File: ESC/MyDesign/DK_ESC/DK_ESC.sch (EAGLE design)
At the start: 38 parts

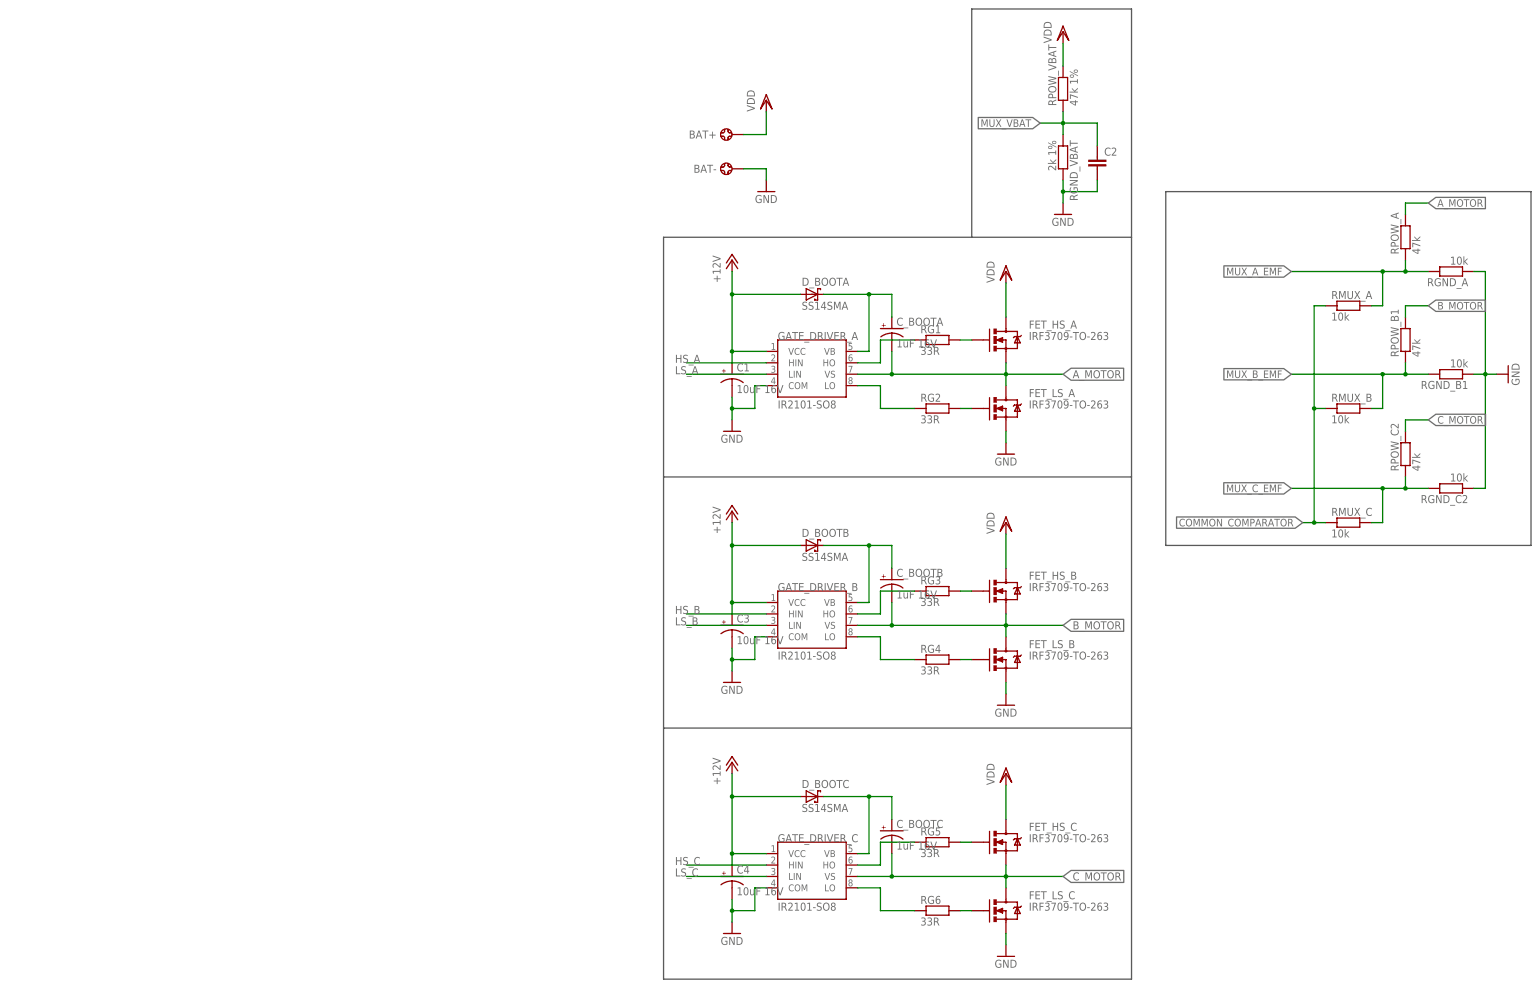
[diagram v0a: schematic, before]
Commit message: ESC Design: include MCU
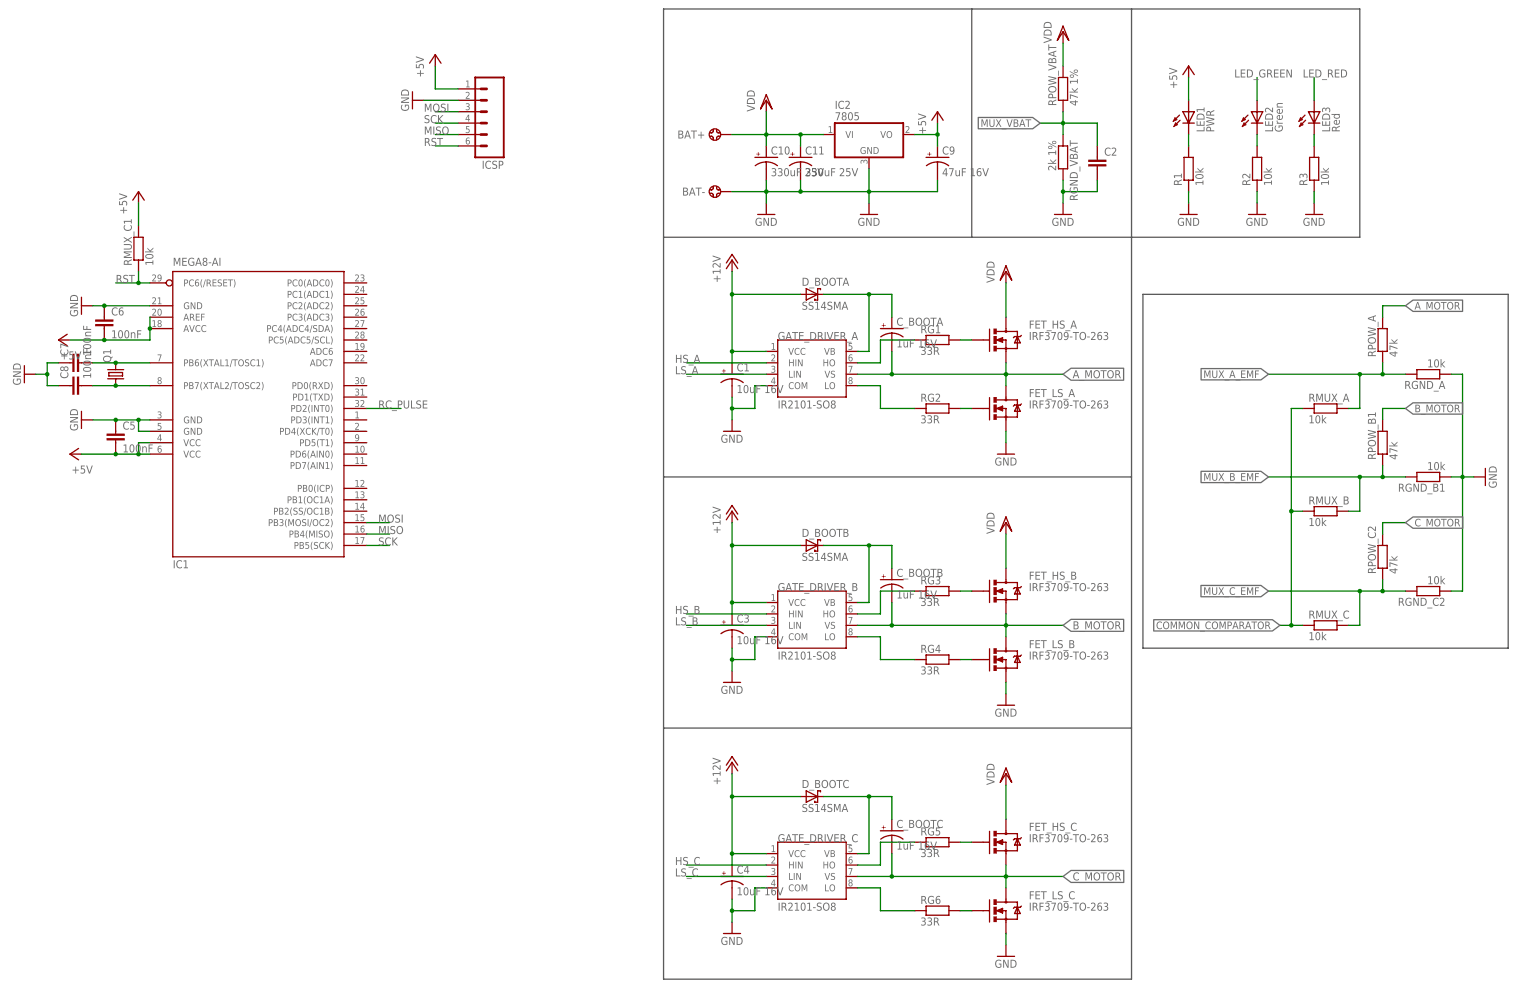
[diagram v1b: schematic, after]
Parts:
- added C10, C11: 330uF 25V, DangKiet:CAP_POLPTH
- added C5, C6, C7, C8: 100nF, RCL:C-SMDC0805K
- added C9: 47uF 16V, RCL:C-TANT-SMDEIA6032
- added IC1: MEGA8-AI, atmel:MEGA8-AI
- added IC2: 7805, Regulator-linear:78XXX-3P05-TO252
- added ICSP: (no value), SparkFun-Connectors:M06NO_SILK_FEMALE_PTH
- added LED1: PWR, LED:LED3MM
- added LED2: Green, LED:LED3MM
- added LED3: Red, LED:LED3MM
- added Q1: (no value), DangKiet:CRYSTALHC49S
- added R1, R2, R3: 10k, RCL:RESISTOR-SMDR0805
- added RMUX_C1: 10k, RCL:RESISTOR-SMDR0603
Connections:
- new net +5V: C5.2, C6.2, C9.+, IC1.AREF, IC1.AVCC, IC1.VCC@1, IC1.VCC@2, IC2.VO, ICSP.1, LED1.A, RMUX_C1.2
- new net LED_GREEN: LED2.A
- new net LED_RED: LED3.A
- new net MISO: IC1.PB4(MISO), ICSP.5
- new net MOSI: IC1.PB3(MOSI/OC2), ICSP.3
- new net N$13: LED1.C, R1.2
- new net N$14: C7.2, IC1.PB6(XTAL1/TOSC1), Q1.2
- new net N$15: C8.2, IC1.PB7(XTAL2/TOSC2), Q1.1
- new net N$16: LED2.C, R2.2
- new net N$17: LED3.C, R3.2
- new net RC_PULSE: IC1.PD2(INT0)
- new net RST: IC1.PC6(/RESET), ICSP.6, RMUX_C1.1
- new net SCK: IC1.PB5(SCK), ICSP.4
- net GND: now also C10.-, C11.-, C5.1, C6.1, C7.1, C8.1, C9.-, IC1.GND, IC1.GND@1, IC1.GND@2, IC2.GND, ICSP.2, R1.1, R2.1, R3.1
- net VDD: now also C10.+, C11.+, IC2.VI
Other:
- note added: "HALF-BRIDGE"
- note added: "POWER SUPPLY"
- moved on the sheet: BAT+, BAT-, RGND_A, RGND_B1, RGND_C2, RMUX_A, RMUX_B, RMUX_C, RPOW_A, RPOW_B1, RPOW_C2

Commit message: Update layout ESC: test version
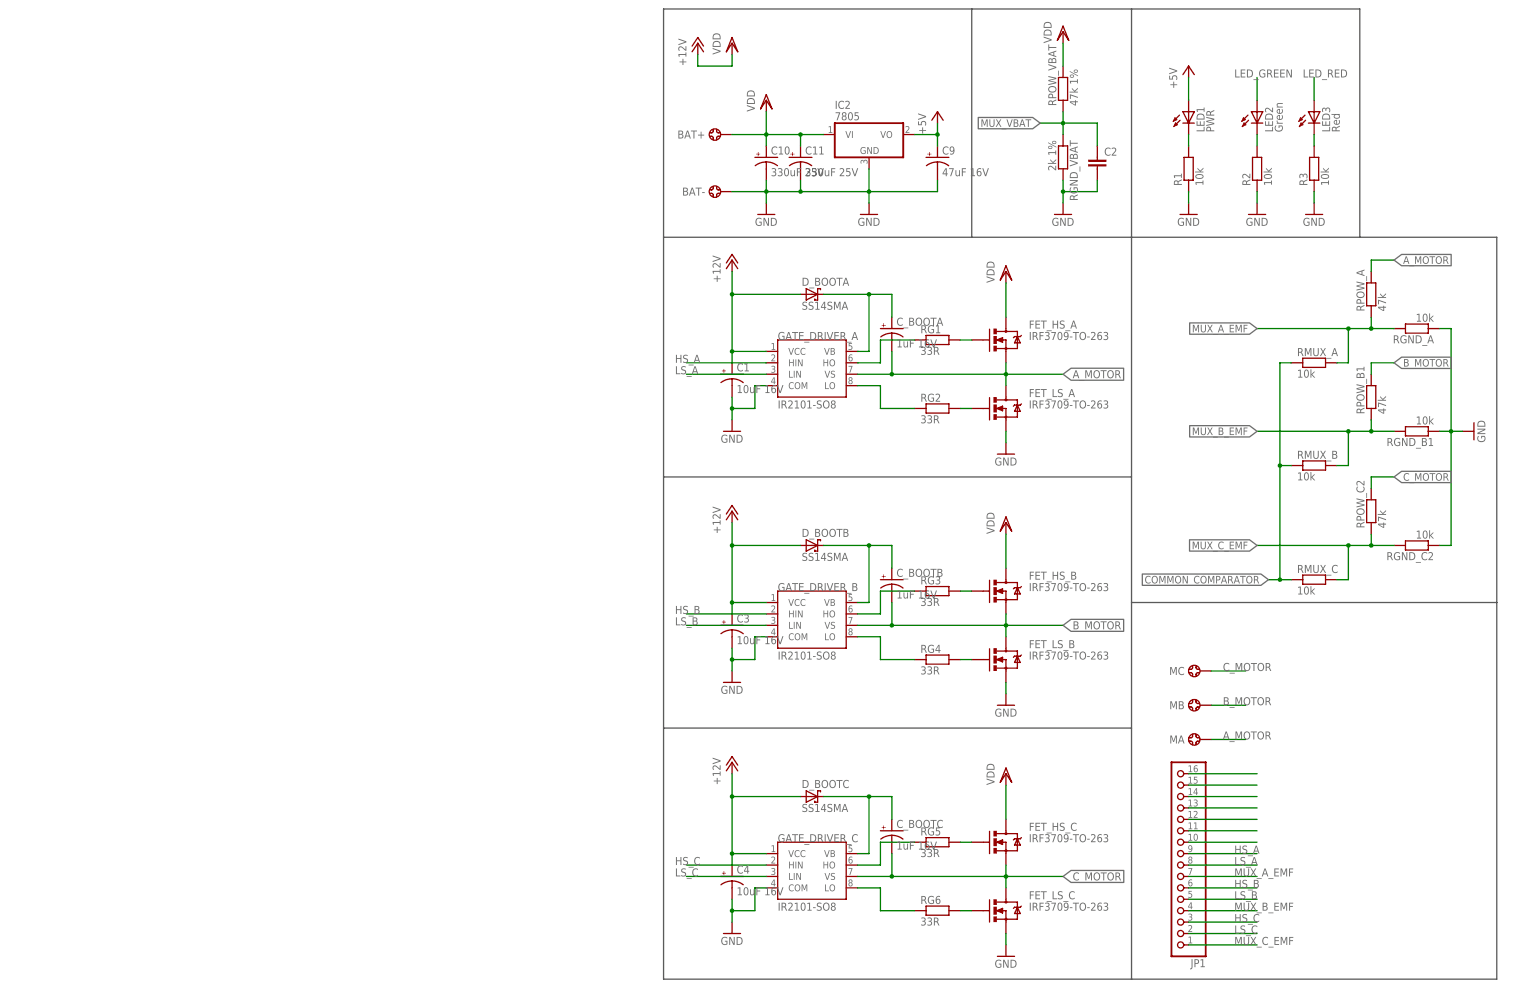
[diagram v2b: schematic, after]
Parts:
- removed C5, C6, C7, C8: 100nF, RCL:C-SMDC0805K
- removed IC1: MEGA8-AI, atmel:MEGA8-AI
- removed ICSP: (no value), SparkFun-Connectors:M06NO_SILK_FEMALE_PTH
- removed Q1: (no value), DangKiet:CRYSTALHC49S
- removed RMUX_C1: 10k, RCL:RESISTOR-SMDR0603
- added JP1: (no value), pinhead:PINHD-1X16
- added MA, MB, MC: 14AWG_PAD-PAD, Connector:14AWG_PAD-PAD
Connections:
- removed net MISO: IC1.PB4(MISO), ICSP.5
- removed net MOSI: IC1.PB3(MOSI/OC2), ICSP.3
- removed net RC_PULSE: IC1.PD2(INT0)
- removed net RST: IC1.PC6(/RESET), ICSP.6, RMUX_C1.1
- removed net SCK: IC1.PB5(SCK), ICSP.4
- new net N$18: JP1.14
- new net N$19: JP1.13
- new net N$20: JP1.12
- new net N$21: JP1.11
- new net N$22: JP1.10
- net +5V: no longer C5.2, C6.2, IC1.AREF, IC1.AVCC, IC1.VCC@1, IC1.VCC@2, ICSP.1, RMUX_C1.2
- net A_MOTOR: now also MA.1
- net B_MOTOR: now also MB.1
- net C_MOTOR: now also MC.1
- net GND: no longer C5.1, C6.1, C7.1, C8.1, IC1.GND, IC1.GND@1, IC1.GND@2, ICSP.2
- net HS_A: now also JP1.9
- net HS_B: now also JP1.6
- net HS_C: now also JP1.3
- net LS_A: now also JP1.8
- net LS_B: now also JP1.5
- net LS_C: now also JP1.2
- net MUX_A_EMF: now also JP1.7
- net MUX_B_EMF: now also JP1.4
- net MUX_C_EMF: now also JP1.1
- net N$14: now also JP1.16; no longer C7.2, IC1.PB6(XTAL1/TOSC1), Q1.2
- net N$15: now also JP1.15; no longer C8.2, IC1.PB7(XTAL2/TOSC2), Q1.1
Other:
- note added: "CONNECTOR"
- moved on the sheet: RGND_A, RGND_B1, RGND_C2, RMUX_A, RMUX_B, RMUX_C, RPOW_A, RPOW_B1, RPOW_C2

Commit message: Add Datasheet mosfet and update layout test ESC
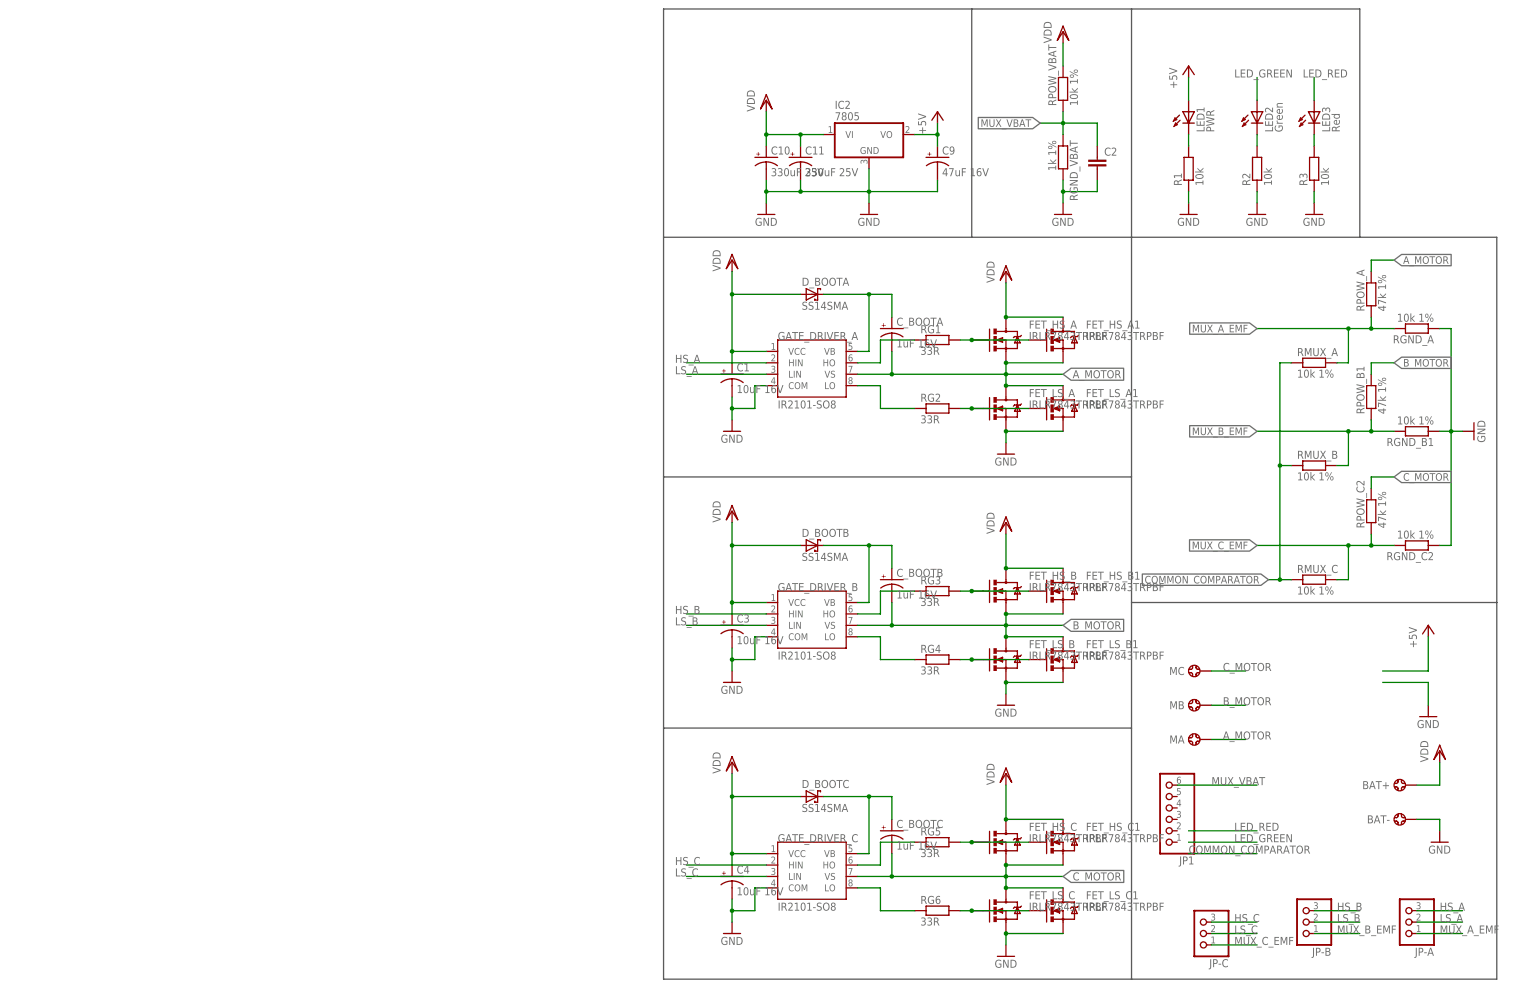
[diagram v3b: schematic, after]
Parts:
- added FET_HS_A1, FET_HS_B1, FET_HS_C1, FET_LS_A1, FET_LS_B1, FET_LS_C1: IRLR7843TRPBF, FET:IRLR7843TRPBF-DPAK
- added JP-A, JP-B, JP-C: (no value), pinhead:PINHD-1X3
- FET_HS_A, FET_HS_B, FET_HS_C, FET_LS_A, FET_LS_B, FET_LS_C: value IRF3709-TO-263 -> IRLR7843TRPBF; device FET:IRF3709-TO-263 -> FET:IRLR7843TRPBF-DPAK
- JP1: device pinhead:PINHD-1X16 -> pinhead:PINHD-1X6
- LED1, LED2, LED3: device LED:LED3MM -> LED:LED0805
- RGND_A, RGND_B1, RGND_C2, RMUX_A, RMUX_B, RMUX_C: value 10k -> 10k 1%; device RCL:RESISTOR-SMDR0603 -> RCL:RESISTOR-SMDR0805
- RGND_VBAT: value 2k 1% -> 1k 1%; device RCL:RESISTOR-SMDR0603 -> RCL:RESISTOR-SMDR0805
- RPOW_A, RPOW_B1, RPOW_C2: value 47k -> 47k 1%
- RPOW_VBAT: value 47k 1% -> 10k 1%; device RCL:RESISTOR-SMDR0603 -> RCL:RESISTOR-SMDR0805
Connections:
- removed net +12V: C1.+, C3.+, C4.+, D_BOOTA.A, D_BOOTB.A, D_BOOTC.A, GATE_DRIVER_A.VCC, GATE_DRIVER_B.VCC, GATE_DRIVER_C.VCC
- removed net COM: C1.-, C3.-, C4.-, GATE_DRIVER_A.COM, GATE_DRIVER_B.COM, GATE_DRIVER_C.COM
- removed net N$14: JP1.16
- removed net N$15: JP1.15
- removed net N$18: JP1.14
- removed net N$19: JP1.13
- removed net N$20: JP1.12
- removed net N$21: JP1.11
- removed net N$22: JP1.10
- net A_MOTOR: now also FET_HS_A1.S, FET_LS_A1.D
- net B_MOTOR: now also FET_HS_B1.S, FET_LS_B1.D
- net C_MOTOR: now also FET_HS_C1.S, FET_LS_C1.D
- net GND: now also C1.-, C3.-, C4.-, FET_LS_A1.S, FET_LS_B1.S, FET_LS_C1.S, GATE_DRIVER_A.COM, GATE_DRIVER_B.COM, GATE_DRIVER_C.COM
- net HS_A: now also JP-A.3; no longer JP1.9
- net HS_B: now also JP-B.3; no longer JP1.6
- net HS_C: now also JP-C.3; no longer JP1.3
- net LS_A: now also JP-A.2; no longer JP1.8
- net LS_B: now also JP-B.2; no longer JP1.5
- net LS_C: now also JP-C.2; no longer JP1.2
- net MUX_A_EMF: now also JP-A.1; no longer JP1.7
- net MUX_B_EMF: now also JP-B.1; no longer JP1.4
- net MUX_C_EMF: now also JP-C.1; no longer JP1.1
- net MUX_VBAT: now also JP1.6
- net N$1: now also FET_LS_A1.G
- net N$10: now also FET_HS_C1.G
- net N$2: now also FET_HS_A1.G
- net N$3: now also FET_LS_B1.G
- net N$6: now also FET_HS_B1.G
- net N$9: now also FET_LS_C1.G
- net VDD: now also C1.+, C3.+, C4.+, D_BOOTA.A, D_BOOTB.A, D_BOOTC.A, FET_HS_A1.D, FET_HS_B1.D, FET_HS_C1.D, GATE_DRIVER_A.VCC, GATE_DRIVER_B.VCC, GATE_DRIVER_C.VCC
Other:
- moved on the sheet: BAT+, BAT-
